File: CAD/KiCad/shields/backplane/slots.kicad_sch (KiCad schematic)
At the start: 11 parts

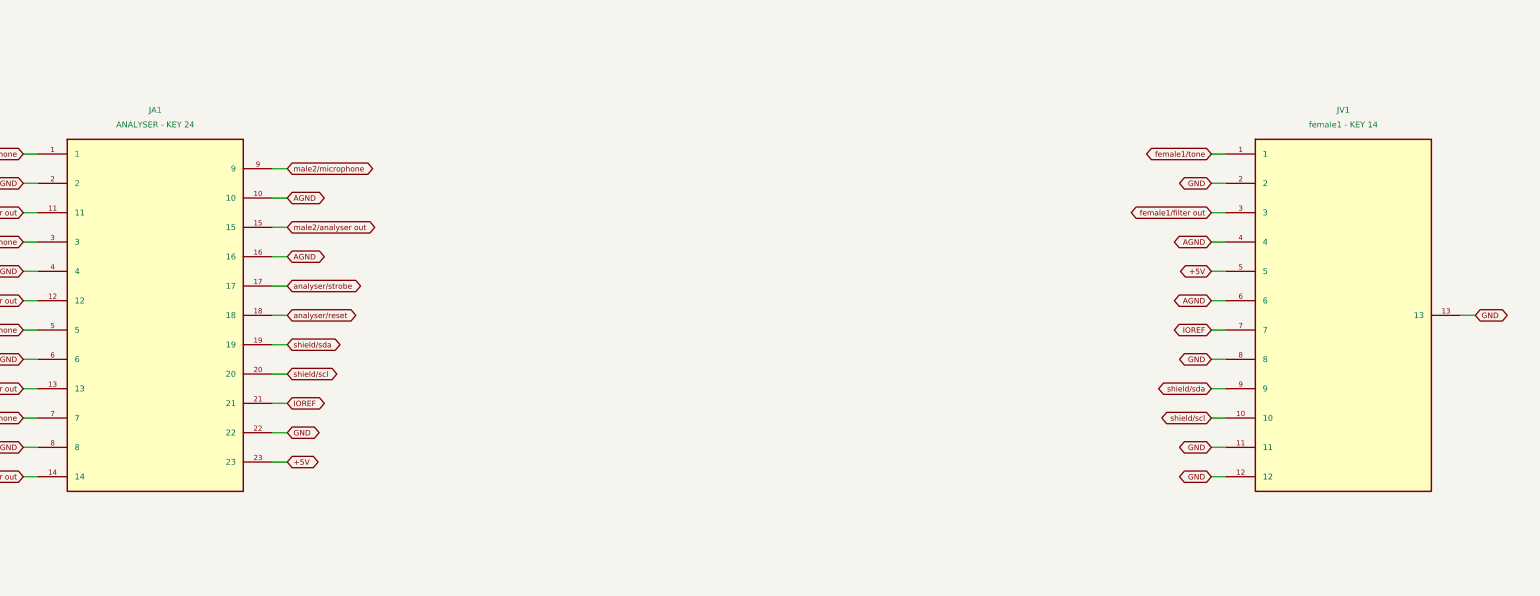
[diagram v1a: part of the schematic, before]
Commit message: Remove shield identification and adopt the simplified connector and Teensy pin maps
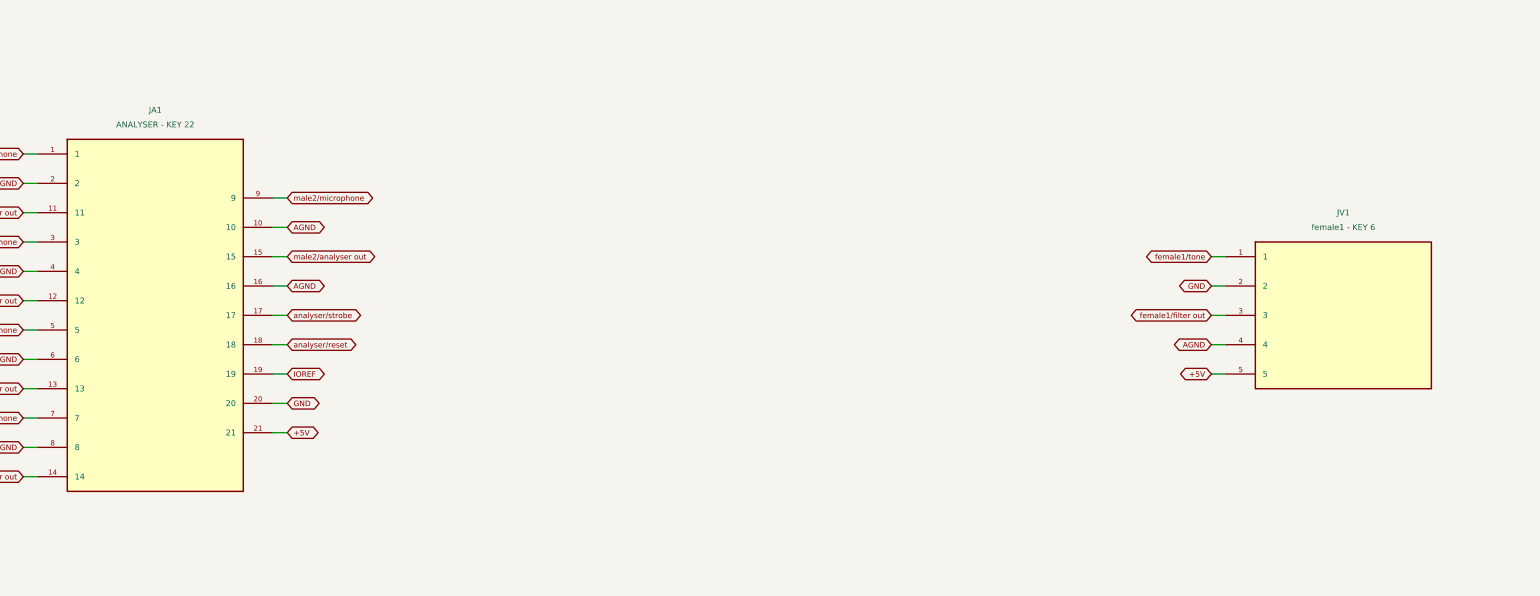
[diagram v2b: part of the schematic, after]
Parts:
- JA1: value ANALYSER - KEY 24 -> ANALYSER - KEY 22; footprint Shields:Header_2x12_Key24 -> Shields:Header_2x11_Key22
- JV1: value female1 - KEY 14 -> female1 - KEY 6; footprint Shields:Header_2x07_Key14 -> Shields:Header_2x03_Key6
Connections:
- net +5V: now also JA1.21; no longer JA1.23
- net AGND: no longer JV1.6
- net GND: now also JA1.20; no longer JA1.22, JV1.11, JV1.12, JV1.13, JV1.8
- net IOREF: now also JA1.19; no longer JA1.21, JV1.7
- removed net shield/scl: JA1.20, JV1.10
- removed net shield/sda: JA1.19, JV1.9

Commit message: Route microphones directly to Teensy and remove the analyser buffer board
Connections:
- net +5V: no longer JA1.21
- net GND: now also JA1.21
- net IOREF renamed MEGA_5V
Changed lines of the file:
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@@
 (kicad_sch (version 20250114) (generator "eeschema") (generator_version "9.0")
  (paper "A3")
-          (title_block (title "backplane / slots") (date "2026-10-04") (rev "A-prototype")
+          (title_block (title "backplane / slots") (date "2026-10-05") (rev "A-prototype")
             (company "Colloquy of Mobiles") (comment 1 "Prototype: verify harness polarity and sensor values before connection"))
           (text "COLLOQUY / BACKPLANE / SLOTS" (at 15.24 15.24 0) (effects (font (size 2.032 2.032) (bold yes)) (justify left top)))
@@
 (global_label "analyser/reset" (shape bidirectional) (at 124.4600 88.9000 0) (effects (font (size 0.95 0.95)) (justify left)) (property "Intersheetrefs" "${INTERSHEET_REFS}" (at 124.4600 88.9000 0) (effects (font (size 1.016 1.016))  (hide yes))))
 (wire (pts (xy 121.9200 93.9800) (xy 124.4600 93.9800)) (stroke (width 0) (type default)))
-(global_label "IOREF" (shape bidirectional) (at 124.4600 93.9800 0) (effects (font (size 0.95 0.95)) (justify left)) (property "Intersheetrefs" "${INTERSHEET_REFS}" (at 124.4600 93.9800 0) (effects (font (size 1.016 1.016))  (hide yes))))
+(global_label "MEGA_5V" (shape bidirectional) (at 124.4600 93.9800 0) (effects (font (size 0.95 0.95)) (justify left)) (property "Intersheetrefs" "${INTERSHEET_REFS}" (at 124.4600 93.9800 0) (effects (font (size 1.016 1.016))  (hide yes))))
 (wire (pts (xy 121.9200 99.0600) (xy 124.4600 99.0600)) (stroke (width 0) (type default)))
 (global_label "GND" (shape bidirectional) (at 124.4600 99.0600 0) (effects (font (size 0.95 0.95)) (justify left)) (property "Intersheetrefs" "${INTERSHEET_REFS}" (at 124.4600 99.0600 0) (effects (font (size 1.016 1.016))  (hide yes))))
 (wire (pts (xy 121.9200 104.1400) (xy 124.4600 104.1400)) (stroke (width 0) (type default)))
-(global_label "+5V" (shape bidirectional) (at 124.4600 104.1400 0) (effects (font (size 0.95 0.95)) (justify left)) (property "Intersheetrefs" "${INTERSHEET_REFS}" (at 124.4600 104.1400 0) (effects (font (size 1.016 1.016))  (hide yes))))
+(global_label "GND" (shape bidirectional) (at 124.4600 104.1400 0) (effects (font (size 0.95 0.95)) (justify left)) (property "Intersheetrefs" "${INTERSHEET_REFS}" (at 124.4600 104.1400 0) (effects (font (size 1.016 1.016))  (hide yes))))
 (symbol (lib_id "Colloquy:JV1") (at 307.3400 83.8200 0) (unit 1) (exclude_from_sim no) (in_bom yes) (on_board yes) (dnp no)
 (property "Reference" "JV1" (at 307.3400 66.0400 0) (effects (font (size 1.016 1.016))  ))

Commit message: Update shields for Thomas RC cards, debug headers and body microphones
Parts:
- removed TPV1: female1/tone, Shields:TestPoint_Pad_D1.5mm, symbol Colloquy:TPV1
- removed TPV2: female2/tone, Shields:TestPoint_Pad_D1.5mm, symbol Colloquy:TPV2
- removed TPV3: female3/tone, Shields:TestPoint_Pad_D1.5mm, symbol Colloquy:TPV3
- removed TPV4: male1/tone, Shields:TestPoint_Pad_D1.5mm, symbol Colloquy:TPV4
- added TPM1: female1/microphone, Shields:TestPoint_Pad_D1.5mm, symbol Colloquy:TPM1
- added TPM2: female2/microphone, Shields:TestPoint_Pad_D1.5mm, symbol Colloquy:TPM2
- added TPM3: female3/microphone, Shields:TestPoint_Pad_D1.5mm, symbol Colloquy:TPM3
- added TPM4: male1/microphone, Shields:TestPoint_Pad_D1.5mm, symbol Colloquy:TPM4
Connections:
- net female1/microphone: now also TPM1.1
- net female2/microphone: now also TPM2.1
- net female3/microphone: now also TPM3.1
- net male1/microphone: now also TPM4.1
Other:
- moved on the sheet: RL2, RL3, RL4, RL5
